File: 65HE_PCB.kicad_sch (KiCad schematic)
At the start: 30 parts, among them J001 JST_SH, SW1 BOOT, SW2 NRST, U201 TLV75733PDBV, U202 TLV75733PDBV, U301 STM32F072CBTx

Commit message: initial commit
i made the board yay!
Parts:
- removed C304: 100nF, Capacitor_SMD:C_0805_2012Metric, symbol Device:C_Small
- removed H1, H2, H3, H4, H5, H6, H7, H8: m2, MountingHole:MountingHole_2.2mm_M2_Pad, symbol Mechanical:MountingHole_Pad_MP
- removed SW1: BOOT, PCM_marbastlib-various:SW_SPST_SKQG_WithStem, symbol Switch:SW_SPST
- removed SW2: NRST, PCM_marbastlib-various:SW_SPST_SKQG_WithStem, symbol Switch:SW_SPST
- removed U202: TLV75733PDBV, Package_TO_SOT_SMD:SOT-23-5, symbol Regulator_Linear:TLV75733PDBV
- removed U301: STM32F072CBTx, Package_QFP:LQFP-48_7x7mm_P0.5mm, symbol MCU_ST_STM32F0:STM32F072CBTx
- added BOOT0, NRST1: SW_SPST, PCM_marbastlib-various:SW_SPST_SKQG_WithStem, symbol Switch:SW_SPST
- added C303: 1uF, Capacitor_SMD:C_1206_3216Metric, symbol Device:C_Small
- added C401, C402: 30pF, Capacitor_SMD:C_0603_1608Metric, symbol Device:C_Small
- added FID1, FID2, FID3: Fiducial, Fiducial:Fiducial_1mm_Mask2mm, symbol Mechanical:Fiducial
- added H1, H2, H3, H4: m2, MountingHole:MountingHole_2.2mm_M2_Pad, symbol Mechanical:MountingHole_Pad
- added U201: XC6206PxxxMR, Package_TO_SOT_SMD:SOT-23-3, symbol Regulator_Linear:XC6206PxxxMR
- added U301: AT32F405CCT7, Package_QFP:LQFP-48_7x7mm_P0.5mm, symbol PCM_marbastlib-various:AT32F405CCT7
- added Y1: X322512MSB4SI, Crystal:Crystal_SMD_3225-4Pin_3.2x2.5mm, symbol Device:Crystal_GND24
- C201: renamed from C203; value 2.2uF -> 1uF
- C202: renamed from C204; value 2.2uF -> 1uF
- D001, R001: now left out of the parts list
- R301, R302: value 5.1KΩ -> 12kΩ
- renumbered C201 to C203, C202 to C204, C305 to C302, C302 to C304, C303 to C305, U201 to U202
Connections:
- net +3.3V: now also C202.2, BOOT0.2 (B), U201.2 (VO), U301.1 (VDD), U301.28 (VDD), U301.48 (VDD); no longer C204.2, U202.5 (OUT)
- net +3.3VA: now also C204.2, U202.5 (OUT), C303.1, U301.9 (VDDA); no longer C202.2
- net +5V: now also U201.3 (VI)
- net D+: now also U301.27 (DP)
- net D-: now also U301.26 (DM)
- net GND: now also R301.2, C303.2, C401.1, C402.1, NRST1.2 (B), U201.1 (GND), U301.23 (VSS), U301.47 (VSS), U301.8 (VSSA), Y1.2, Y1.4
- net RST: now reaches C306.2
- net RST: now also NRST1.1 (A), U301.7 (~{RST})
- net BOOT: now reaches R302.2
- net BOOT: now also BOOT0.1 (A), U301.44 (PF11/BOOT0); no longer R301.1
- new net HS_R: R301.1, U301.25 (HS_R)
- new net MUX_OUT_1: U301.10 (PA0)
- new net MUX_OUT_10: U301.19 (PB1)
- new net MUX_OUT_2: U301.11 (PA1)
- new net MUX_OUT_3: U301.12 (PA2)
- new net MUX_OUT_4: U301.13 (PA3)
- new net MUX_OUT_5: U301.14 (PA4)
- new net MUX_OUT_6: U301.15 (PA5)
- new net MUX_OUT_7: U301.16 (PA6)
- new net MUX_OUT_8: U301.17 (PA7)
- new net MUX_OUT_9: U301.18 (PB0)
- new net MUX_SEL_1: U301.2 (PC13)
- new net MUX_SEL_2: U301.3 (PC14)
- new net MUX_SEL_3: U301.4 (PC15)
- new net OSC_IN: C402.2, U301.5 (PF0), Y1.3
- new net OSC_OUT: C401.2, U301.6 (PF1), Y1.1
- no-connect marks 13 -> 4
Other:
- note added: "4xx"
- note added: "Crystal Oscillator"
- note added: "Fiducial Markers"
- note added: "I used the same 12k ohm resistor as needed for the HS_R as the pullup resistor here for bom reduction"
- note added: "not implemented in the pcb"
- moved on the sheet: C201, C202, C203, C204, C301, C302, C304, C305, U202

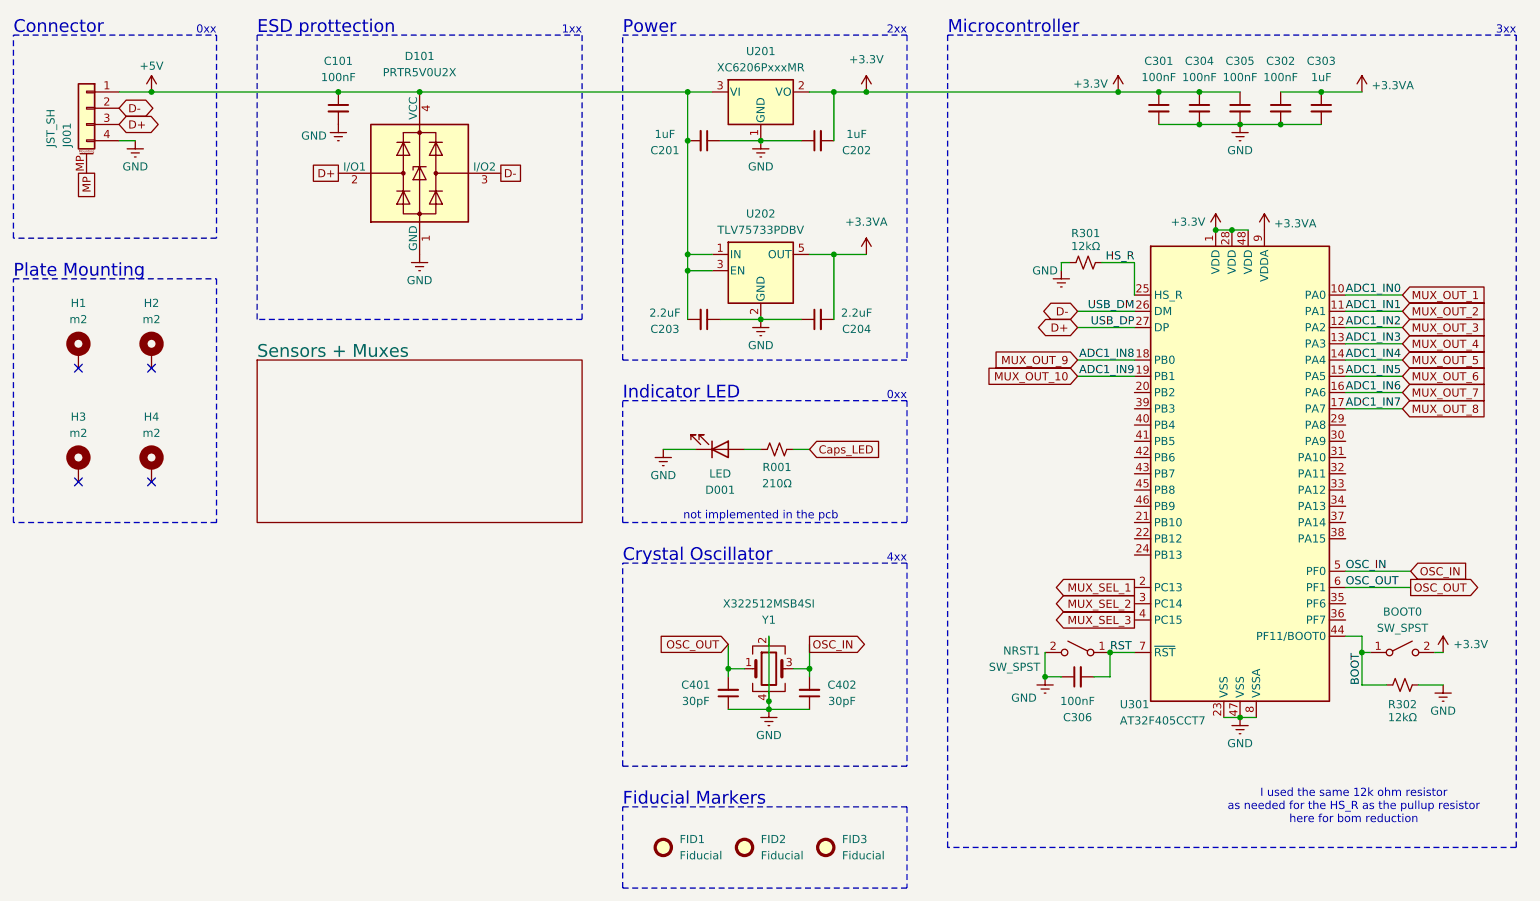
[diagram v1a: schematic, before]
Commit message: no rounded tracks
routed the pcb again but without rounding the tracks because kicad became laggy af
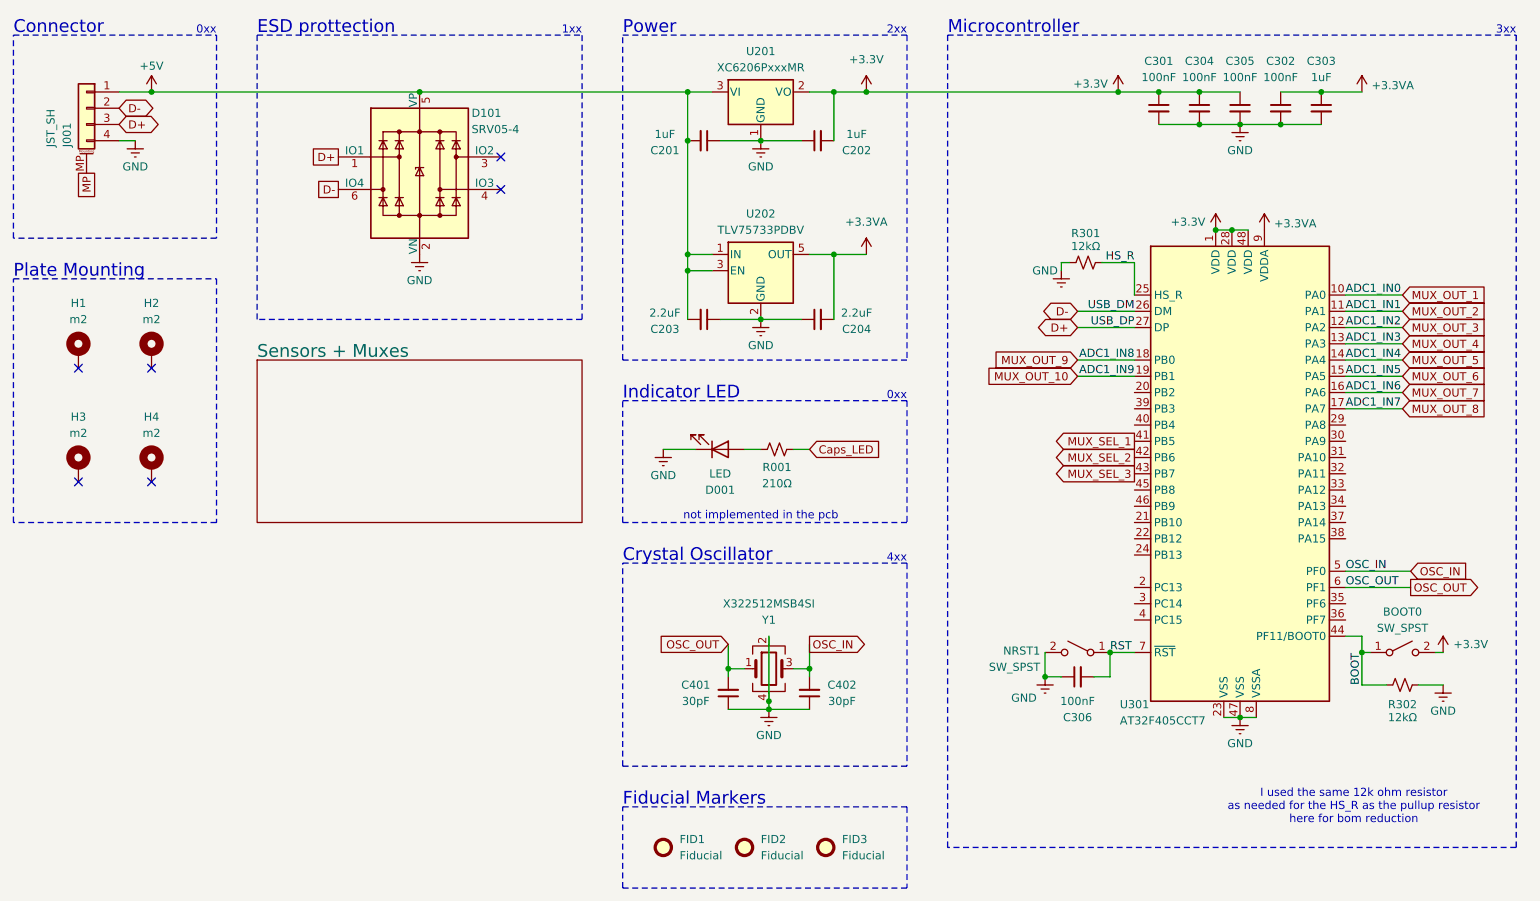
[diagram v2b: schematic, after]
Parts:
- removed C101: 100nF, Capacitor_SMD:C_0805_2012Metric, symbol Device:C_Small
- removed D101: PRTR5V0U2X, Package_TO_SOT_SMD:SOT-143, symbol Power_Protection:PRTR5V0U2X
- added D101: SRV05-4, PCM_marbastlib-various:SOT-23-6-routable, symbol PCM_marbastlib-various:SRV05-4
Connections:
- net +5V: now also D101.5 (VP)
- net D+: now also D101.1 (IO1)
- net D-: now also D101.6 (IO4)
- net GND: now also D101.2 (VN)
- net MUX_SEL_1: now also U301.41 (PB5); no longer U301.2 (PC13)
- net MUX_SEL_2: now also U301.42 (PB6); no longer U301.3 (PC14)
- net MUX_SEL_3: now also U301.43 (PB7); no longer U301.4 (PC15)
- no-connect marks 4 -> 6
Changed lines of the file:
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@@
 	)
 	(junction
-		(at 160.02 59.69)
+		(at 95.25 34.29)
 		(diameter 0)
 		(color 0 0 0 0)
 	)
 	(junction
-		(at 236.22 34.29)
+		(at 160.02 59.69)
 		(diameter 0)
 		(color 0 0 0 0)
 	)
 	(junction
-		(at 222.25 55.88)
+		(at 236.22 34.29)
 		(diameter 0)
 		(color 0 0 0 0)
 	)
 	(junction
-		(at 148.59 69.85)
+		(at 222.25 55.88)
 		(diameter 0)
 		(color 0 0 0 0)
 	)
 	(junction
-		(at 95.25 34.29)
+		(at 148.59 69.85)
 		(diameter 0)
 		(color 0 0 0 0)
@@
 	)
 	(junction
-		(at 82.55 34.29)
-		(diameter 0)
-		(color 0 0 0 0)
-	)
-	(junction
 		(at 160.02 34.29)
 		(diameter 0)
@@
 	)
 	(no_connect
+		(at 107.95 44.45)
+	)
+	(no_connect
 		(at 53.34 95.25)
 	)
@@
 		(at 53.34 77.47)
 	)
+	(no_connect
+		(at 107.95 49.53)
+	)
 	(wire
 		(pts
@@
 	(wire
 		(pts
-			(xy 53.34 34.29) (xy 82.55 34.29)
+			(xy 95.25 34.29) (xy 137.16 34.29)
 		)
 		(stroke
@@
 	(wire
 		(pts
-			(xy 95.25 34.29) (xy 137.16 34.29)
+			(xy 53.34 34.29) (xy 95.25 34.29)
 		)
 		(stroke
@@
 	(wire
 		(pts
-			(xy 82.55 34.29) (xy 95.25 34.29)
-		)
-		(stroke
-			(width 0)
-			(type default)
-		)
-	)
-	(wire
-		(pts
 			(xy 137.16 59.69) (xy 140.97 59.69)
 		)
@@
 	(global_label "MUX_SEL_3"
 		(shape output)
-		(at 207.01 116.84 180)
+		(at 207.01 93.98 180)
 		(fields_autoplaced yes)
 		(effects
@@
 		)
 		(property "Intersheetrefs" "${INTERSHEET_REFS}"
-			(at 193.5021 116.84 0)
+			(at 193.5021 93.98 0)
 			(effects
 				(font
@@
 	(global_label "MUX_SEL_1"
 		(shape output)
-		(at 207.01 111.76 180)
+		(at 207.01 88.9 180)
 		(fields_autoplaced yes)
 		(effects
@@
 		)
 		(property "Intersheetrefs" "${INTERSHEET_REFS}"
-			(at 193.5021 111.76 0)
+			(at 193.5021 88.9 0)
 			(effects
 				(font
@@
 	(global_label "D+"
 		(shape passive)
-		(at 82.55 46.99 180)
+		(at 82.55 44.45 180)
 		(fields_autoplaced yes)
 		(effects
@@
 		)
 		(property "Intersheetrefs" "${INTERSHEET_REFS}"
-			(at 77.8337 46.99 0)
+			(at 77.8337 44.45 0)
 			(effects
 				(font
@@
 	(global_label "D-"
 		(shape passive)
-		(at 107.95 46.99 0)
+		(at 82.55 49.53 180)
 		(fields_autoplaced yes)
 		(effects
@@
 				(size 1.27 1.27)
 			)
-			(justify left)
+			(justify right)
 		)
 		(property "Intersheetrefs" "${INTERSHEET_REFS}"
-			(at 112.6663 46.99 0)
+			(at 77.8337 49.53 0)
 			(effects
 				(font
 					(size 1.27 1.27)
 				)
-				(justify left)
+				(justify right)
 				(hide yes)
 			)
@@
 	(global_label "MUX_SEL_2"
 		(shape output)
-		(at 207.01 114.3 180)
+		(at 207.01 91.44 180)
 		(fields_autoplaced yes)
 		(effects
@@
 		)
 		(property "Intersheetrefs" "${INTERSHEET_REFS}"
-			(at 193.5021 114.3 0)
+			(at 193.5021 91.44 0)
 			(effects
 				(font
@@
 	)
 	(symbol
+		(lib_id "PCM_marbastlib-various:SRV05-4")
+		(at 95.25 46.99 0)
+		(unit 1)
+		(exclude_from_sim no)
+		(in_bom yes)
+		(on_board yes)
+		(dnp no)
+		(property "Reference" "D101"
+			(at 103.378 37.592 0)
+			(effects
+				(font
+					(size 1.27 1.27)
+				)
+				(justify left)
+			)
+		)
+		(property "Value" "SRV05-4"
+			(at 103.378 40.132 0)
+			(effects
+				(font
+					(size 1.27 1.27)
+				)
+				(justify left)
+			)
+		)
+		(property "Footprint" "PCM_marbastlib-various:SOT-23-6-routable"
+			(at 113.03 58.42 0)
+			(effects
+				(font
+					(size 1.27 1.27)
+				)
+				(hide yes)
+			)
+		)
+		(property "Datasheet" "http://www.onsemi.com/pub/Collateral/SRV05-4-D.PDF"
+			(at 95.25 46.99 0)
+			(effects
+				(font
+					(size 1.27 1.27)
+				)
+				(hide yes)
+			)
+		)
+		(property "Description" "ESD Protection Diodes with Low Clamping Voltage, SOT-23-6"
+			(at 95.25 46.99 0)
+			(effects
+				(font
+					(size 1.27 1.27)
+				)
+				(hide yes)
+			)
+		)
+		(pin "3"
+		)
+		(pin "2"
+		)
+		(pin "4"
+		)
+		(pin "6"
+		)
+		(pin "1"
+		)
+		(pin "5"
+		)
+		(instances
+			(project ""
+				(path "/9f66ba49-1f22-4b6f-a8b4-c29b9684ab2a"
+					(reference "D101")
+					(unit 1)
+				)
+			)
+		)
+	)
+	(symbol
 		(lib_id "Device:R_Small_US")
 		(at 248.92 127 270)
@@
 	)
 	(symbol
-		(lib_id "Device:C_Small")
-		(at 82.55 36.83 0)
-		(unit 1)
-		(exclude_from_sim no)
-		(in_bom yes)
-		(on_board yes)
-		(dnp no)
-		(property "Reference" "C101"
-			(at 82.55 29.464 0)
-			(effects
-				(font
-					(size 1.27 1.27)
-				)
-			)
-		)
-		(property "Value" "100nF"
-			(at 82.55 32.004 0)
-			(effects
-				(font
-					(size 1.27 1.27)
-				)
-			)
-		)
-		(property "Footprint" "Capacitor_SMD:C_0805_2012Metric"
-			(at 82.55 36.83 0)
-			(effects
-				(font
-					(size 1.27 1.27)
-				)
-				(hide yes)
-			)
-		)
-		(property "Datasheet" "~"
-			(at 82.55 36.83 0)
-			(effects
-				(font
-					(size 1.27 1.27)
-				)
-				(hide yes)
-			)
-		)
-		(property "Description" "Unpolarized capacitor, small symbol"
-			(at 82.55 36.83 0)
-			(effects
-				(font
-					(size 1.27 1.27)
-				)
-				(hide yes)
-			)
-		)
-		(pin "2"
-		)
-		(pin "1"
-		)
-		(instances
-			(project ""
-				(path "/9f66ba49-1f22-4b6f-a8b4-c29b9684ab2a"
-					(reference "C101")
-					(unit 1)
-				)
-			)
-		)
-	)
-	(symbol
 		(lib_id "power:+5V")
 		(at 53.34 34.29 0)
@@
 	)
 	(symbol
-		(lib_id "power:Earth")
-		(at 82.55 39.37 0)
-		(mirror y)
-		(unit 1)
-		(exclude_from_sim no)
-		(in_bom yes)
-		(on_board yes)
-		(dnp no)
-		(property "Reference" "#PWR06"
-			(at 82.55 45.72 0)
-			(effects
-				(font
-					(size 1.27 1.27)
-				)
-				(hide yes)
-			)
-		)
-		(property "Value" "GND"
-			(at 78.74 41.148 0)
-			(effects
-				(font
-					(size 1.27 1.27)
-				)
-			)
-		)
-		(property "Footprint" ""
-			(at 82.55 39.37 0)
-			(effects
-				(font
-					(size 1.27 1.27)
-				)
-				(hide yes)
-			)
-		)
-		(property "Datasheet" "~"
-			(at 82.55 39.37 0)
-			(effects
-				(font
-					(size 1.27 1.27)
-				)
-				(hide yes)
-			)
-		)
-		(property "Description" "Power symbol creates a global label with name \"Earth\""
-			(at 82.55 39.37 0)
-			(effects
-				(font
-					(size 1.27 1.27)
-				)
-				(hide yes)
-			)
-		)
-		(pin "1"
-		)
-		(instances
-			(project "65HE_PCB"
-				(path "/9f66ba49-1f22-4b6f-a8b4-c29b9684ab2a"
-					(reference "#PWR06")
-					(unit 1)
-				)
-			)
-		)
-	)
-	(symbol
 		(lib_id "Switch:SW_SPST")
 		(at 198.12 121.92 0)
@@
 					(unit 1)
 				)
-			)
-		)
-	)
-	(symbol
-		(lib_id "Power_Protection:PRTR5V0U2X")
-		(at 95.25 46.99 0)
-		(unit 1)
-		(exclude_from_sim no)
-		(in_bom yes)
-		(on_board yes)
-		(dnp no)
-		(property "Reference" "D101"
-			(at 95.25 28.702 0)
-			(effects
-				(font
-					(size 1.27 1.27)
-				)
-			)
-		)
-		(property "Value" "PRTR5V0U2X"
-			(at 95.25 31.242 0)
-			(effects
-				(font
-					(size 1.27 1.27)
-				)
-			)
-		)
-		(property "Footprint" "Package_TO_SOT_SMD:SOT-143"
-			(at 96.774 46.99 0)
-			(effects
-				(font
-					(size 1.27 1.27)
-				)
-				(hide yes)
-			)
-		)
-		(property "Datasheet" "https://assets.nexperia.com/documents/data-sheet/PRTR5V0U2X.pdf"
-			(at 96.774 46.99 0)
-			(effects
-				(font
-					(size 1.27 1.27)
-				)
-				(hide yes)
-			)
-		)
-		(property "Description" "Ultra low capacitance double rail-to-rail ESD protection diode, SOT-143"
-			(at 95.25 46.99 0)
-			(effects
-				(font
-					(size 1.27 1.27)
-				)
-				(hide yes)
-			)
-		)
-		(pin "1"
-		)
-		(pin "2"
-		)
-		(pin "4"
-		)
-		(pin "3"
-		)
-		(instances
-			(project ""
-				(path "/9f66ba49-1f22-4b6f-a8b4-c29b9684ab2a"
-					(reference "D101")
-					(unit 1)
-				)
